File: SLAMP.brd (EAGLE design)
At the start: 160 x 100 mm, 57 parts, among them IC2 AT42QT1070-SSU, J1 CARA1, J2 CARA4, J3 CARA2, J4 CARA5, J5 CARA3, J6 EXTRA-D10, J7 A0, Q1 2N7002PW, U1 HC_05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

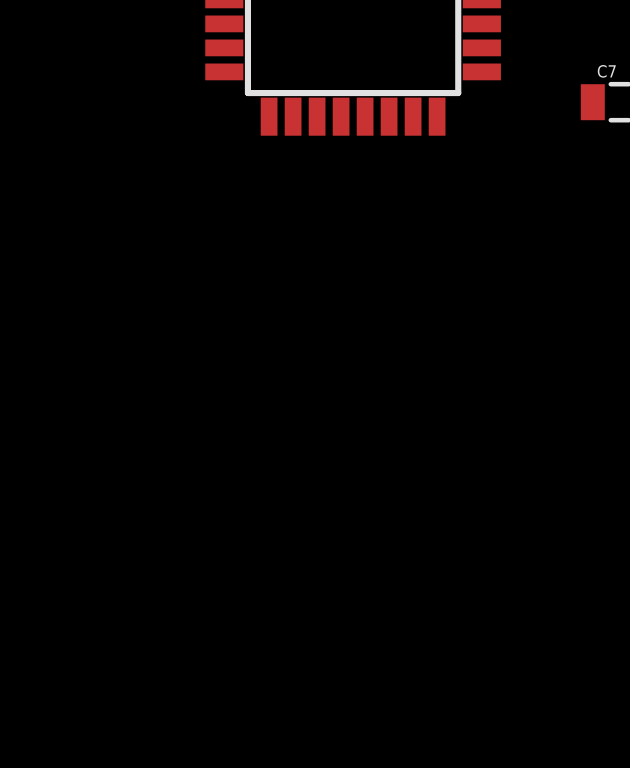
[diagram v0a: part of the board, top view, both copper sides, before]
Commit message: Power control finished
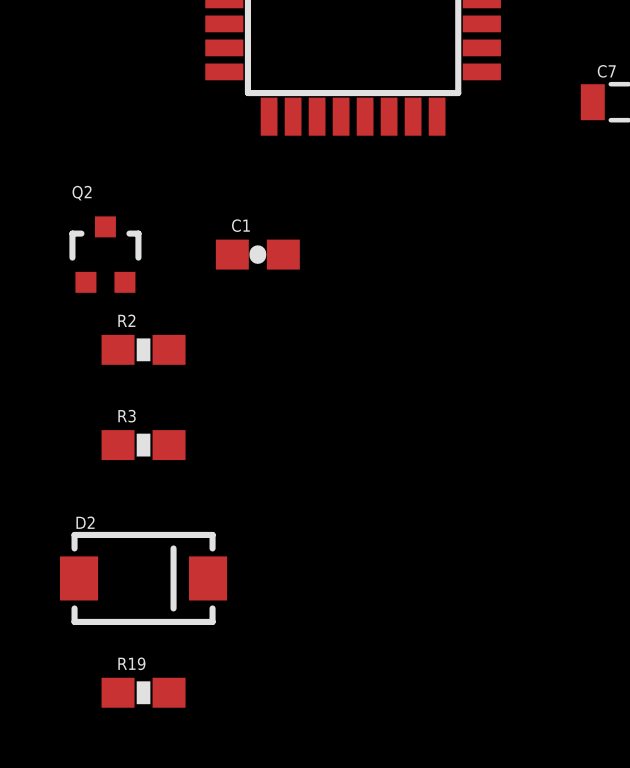
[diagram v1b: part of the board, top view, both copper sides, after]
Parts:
- added C1: 1u, SparkFun-Passives:0603-CAP
- added D2: BA340A, SparkFun-DiscreteSemi:SMA-DIODE
- added Q2: MOSFET-NCHANNEL2N7002PW, SparkFun-DiscreteSemi:SOT323
- added R19, R2: 3.3k, SparkFun-Passives:0603-RES
- added R3: 220, SparkFun-Passives:0603-RES
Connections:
- removed net BT_RX: U1.2, U3.1
- removed net BT_TX: U1.1, U3.32
- new net N$7: Q2.3, R2.1, R3.2
- new net RX_5V: D2.A, D2.C, R19.2, U1.2, U3.1
- new net TX_5V: Q2.2, R3.1, U1.1, U3.32
- net 3.3V: now also C1.1, R19.1
- net 5V: now also Q2.1, R2.2
- net GND: now also C1.2
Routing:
- net RX_5V: track 0.00 -> 83.7 mm, vias 0 -> 5
- net BT_RX: track 83.7 -> 0.00 mm, vias 5 -> 0
- net TX_5V: track 0.00 -> 39.8 mm, vias 0 -> 2
- net BT_TX: track 39.8 -> 0.00 mm, vias 2 -> 0
